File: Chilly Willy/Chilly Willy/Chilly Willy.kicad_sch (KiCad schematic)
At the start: 2 parts, among them J2 Screw_Terminal_01x08, J3 Screw_Terminal_01x03

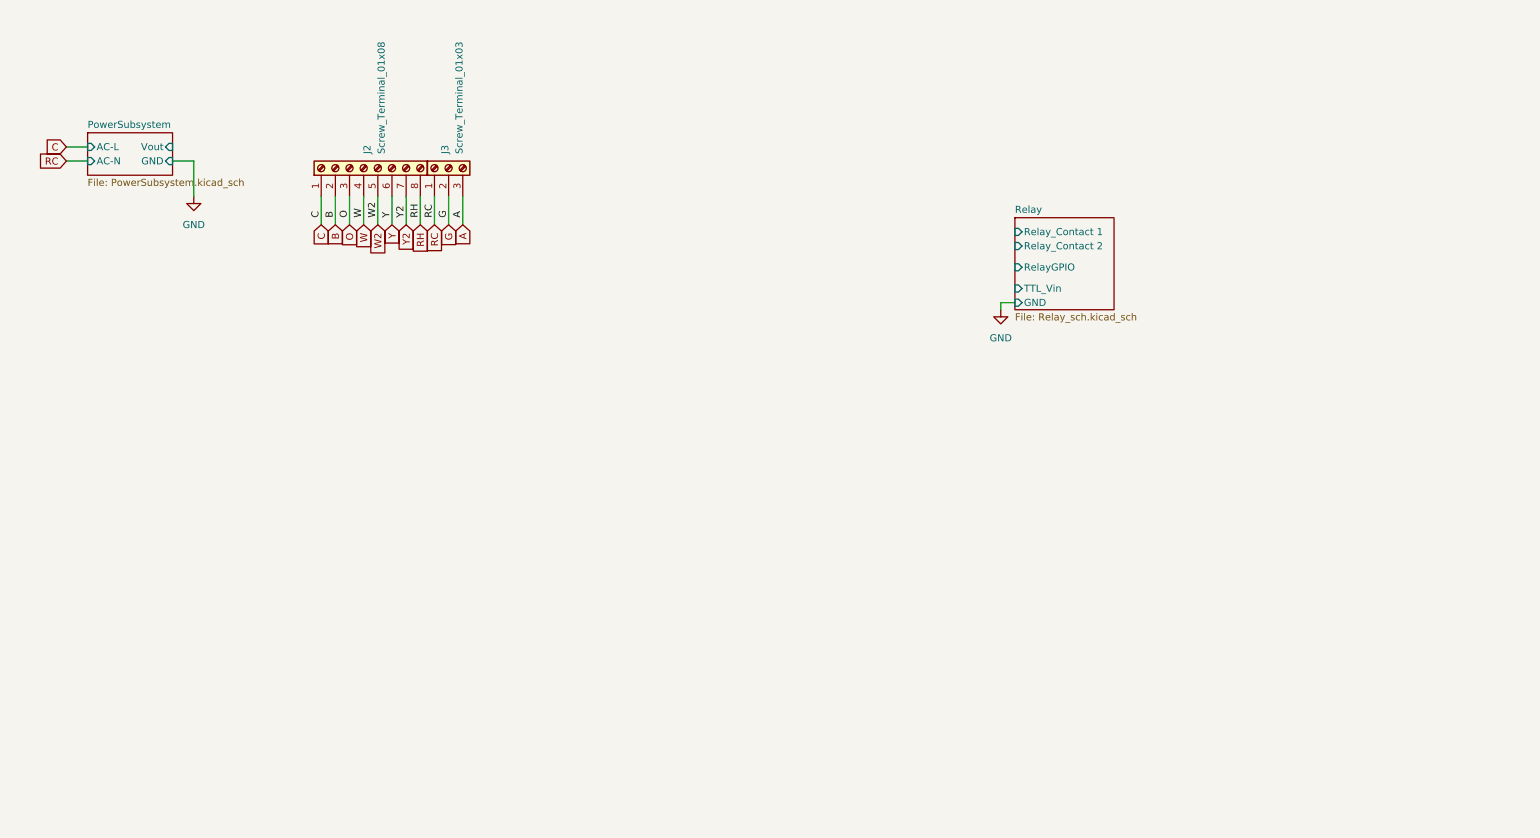
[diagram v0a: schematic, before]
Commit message: * adding in the Relays * GPIO via MCP23008
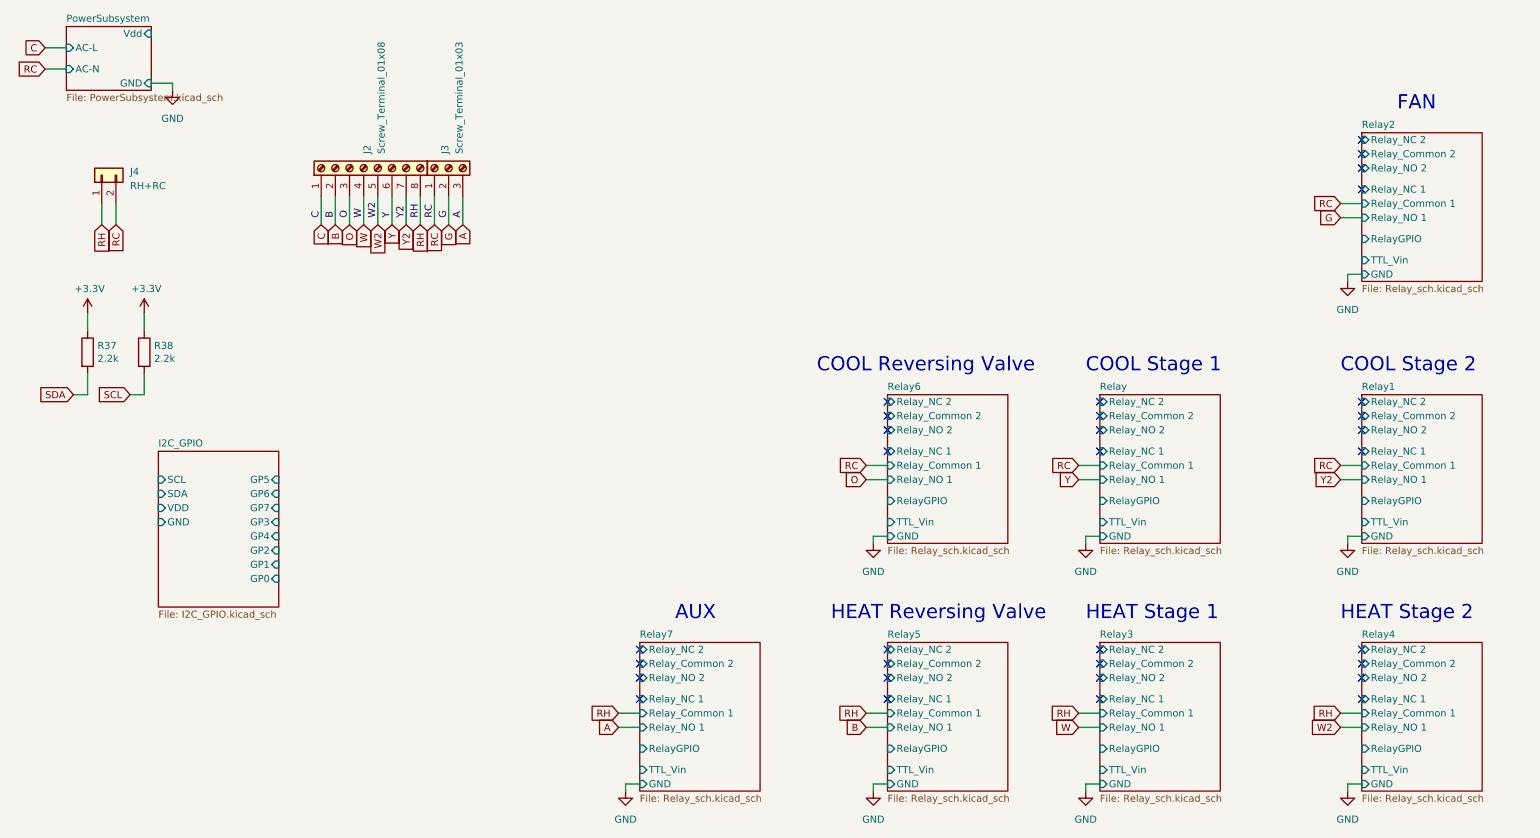
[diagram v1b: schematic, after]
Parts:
- added J4: RH+RC, symbol Connector_Generic:Conn_01x02
- added R37, R38: 2.2k, Resistor_THT:R_Axial_DIN0207_L6.3mm_D2.5mm_P2.54mm_Vertical, symbol Device:R
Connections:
- net RC: now also J4.2 (Pin_2)
- net RH: now also J4.1 (Pin_1)
- new net +3V3: R37.1, R38.1
- new net SCL: R38.2
- new net SDA: R37.2
- no-connect marks 0 -> 32
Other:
- added sheet I2C_GPIO (I2C_GPIO.kicad_sch)
- added sheet Relay1 (Relay_sch.kicad_sch)
- added sheet Relay2 (Relay_sch.kicad_sch)
- added sheet Relay3 (Relay_sch.kicad_sch)
- added sheet Relay4 (Relay_sch.kicad_sch)
- added sheet Relay5 (Relay_sch.kicad_sch)
- added sheet Relay6 (Relay_sch.kicad_sch)
- added sheet Relay7 (Relay_sch.kicad_sch)
- sheet PowerSubsystem ports: added Vdd; removed Vout
- sheet Relay ports: added Relay_Common 1, Relay_Common 2 , Relay_NC 1, Relay_NC 2, Relay_NO 1, Relay_NO 2; removed Relay_Contact 1, Relay_Contact 2
- note added: "AUX"
- note added: "COOL Reversing Valve"
- note added: "COOL Stage 1"
- note added: "COOL Stage 2"
- note added: "FAN"
- note added: "HEAT Reversing Valve"
- note added: "HEAT Stage 1"
- note added: "HEAT Stage 2"

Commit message: ..
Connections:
- no-connect marks 32 -> 0
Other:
- removed sheet Relay
- removed sheet Relay1
- removed sheet Relay2
- removed sheet Relay3
- removed sheet Relay4
- removed sheet Relay5
- removed sheet Relay6
- added sheet Relay10 (Relay_sch.kicad_sch)
- added sheet Relay11 (Relay_sch.kicad_sch)
- added sheet Relay12 (Relay_sch.kicad_sch)
- added sheet Relay13 (Relay_sch.kicad_sch)
- added sheet Relay14 (Relay_sch.kicad_sch)
- added sheet Relay8 (Relay_sch.kicad_sch)
- added sheet Relay9 (Relay_sch.kicad_sch)
- sheet I2C_GPIO ports: added none; removed GP0, GP1, GP2, GP3, GP4, GP5, GP6, GP7
- sheet Relay7 ports: added none; removed Relay_Common 2 , Relay_NC 1, Relay_NC 2, Relay_NO 2
